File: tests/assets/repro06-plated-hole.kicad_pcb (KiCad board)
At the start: 2 copper layers, 50 x 50 mm, 2 parts

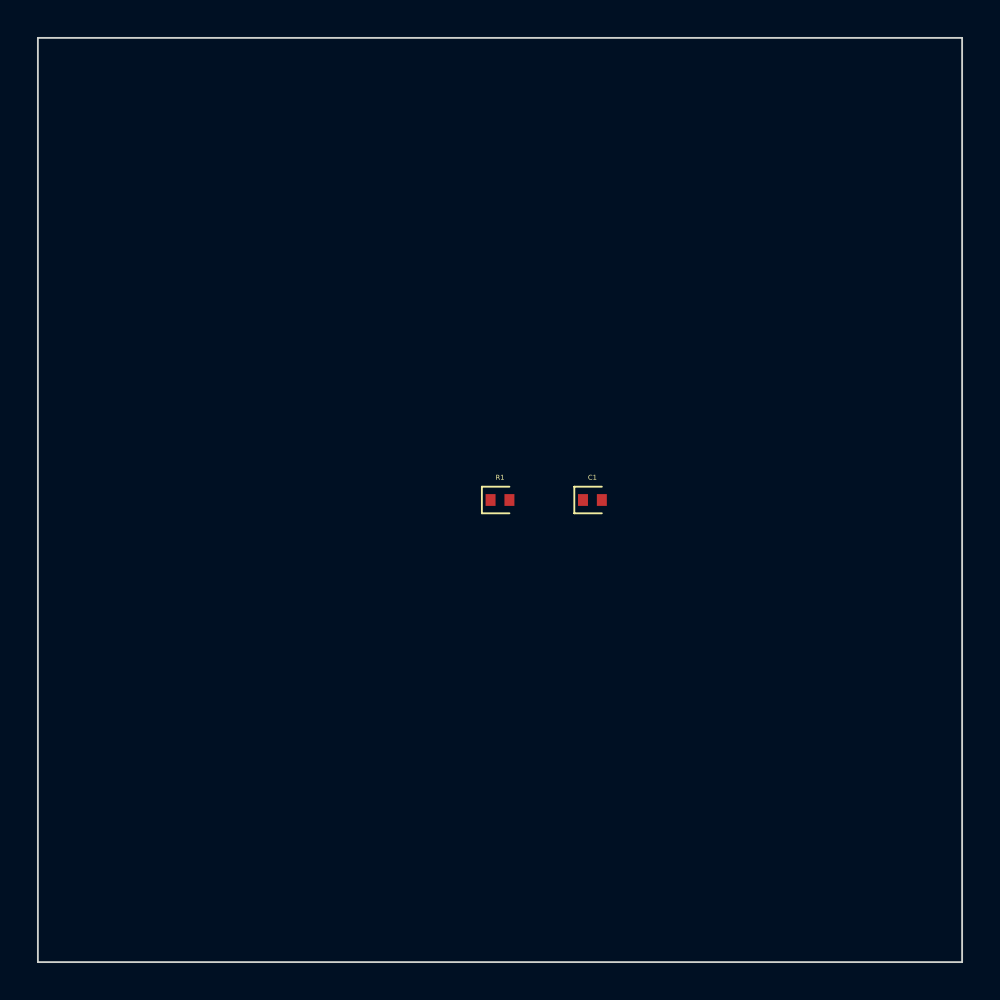
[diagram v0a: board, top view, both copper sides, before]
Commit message: fix: add support for standalone plated holes in KiCad PCB converter (#176)
* fix: add support for standalone plated holes in KiCad PCB converter

* up

* maintain

* remove any
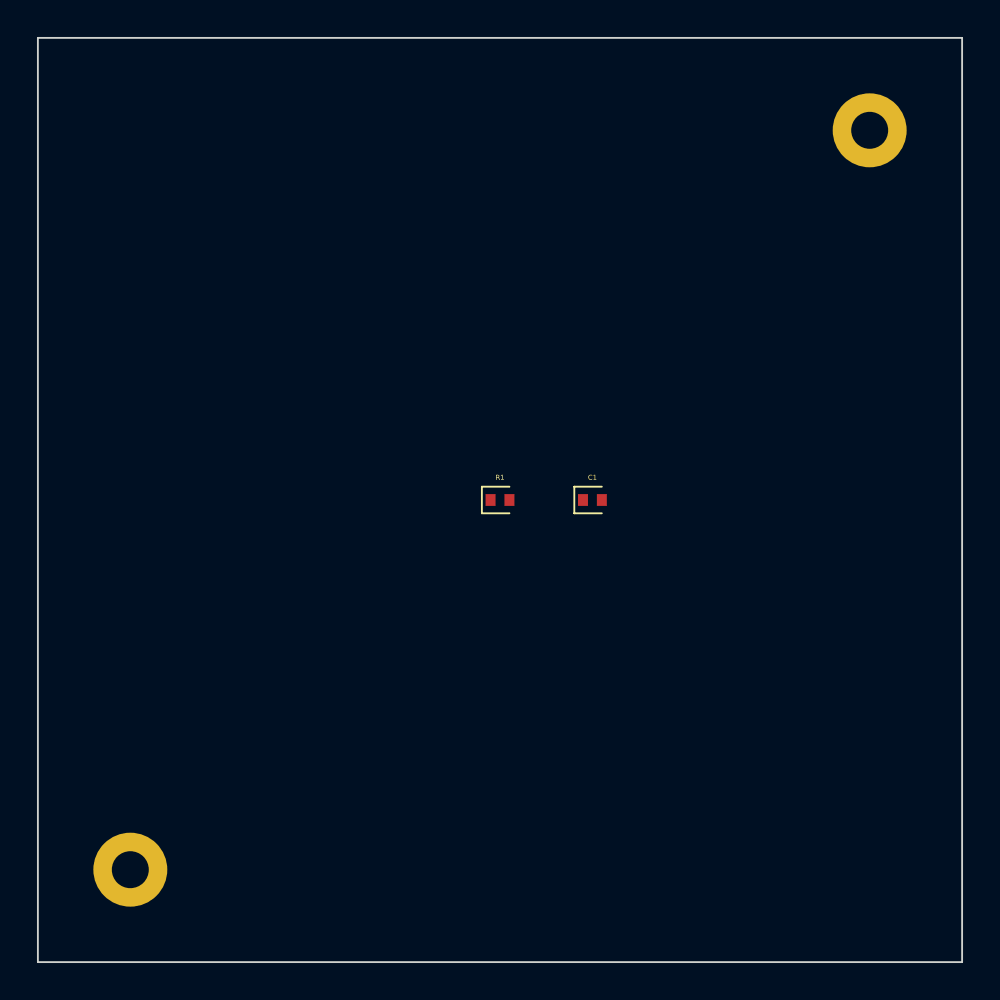
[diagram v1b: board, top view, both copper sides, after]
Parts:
- added ? (x2): , tscircuit:platedhole_circle_holeDiameter2mm_outerDiameter4mm, F.Cu at (100.0, 100.0)
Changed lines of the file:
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@@
+    )
+  )
+  (footprint
+    "tscircuit:platedhole_circle_holeDiameter2mm_outerDiameter4mm"
+    (layer F.Cu)
+    (at 100 100 0)
+    (pad "1" thru_hole circle
+      (at -20 20 0)
+      (size 4 4)
+      (drill 2)
+      (layers *.Cu *.Mask)
+    )
+  )
+  (footprint
+    "tscircuit:platedhole_circle_holeDiameter2mm_outerDiameter4mm"
+    (layer F.Cu)
+    (at 100 100 0)
+    (pad "1" thru_hole circle
+      (at 20 -20 0)
+      (size 4 4)
+      (drill 2)
+      (layers *.Cu *.Mask)
     )
   )
